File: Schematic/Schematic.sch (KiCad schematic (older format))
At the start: 13 parts, among them U1 74LS04, U10 HC-SR04, U11 HC-SR04, U12 HC-SR04, U13 HC-SR04, U2 74LS04, U3 74LS138, U4 ESP32-CAM, U5 HC-SR04, U6 HC-SR04, U7 HC-SR04, U8 HC-SR04, U9 DHT11

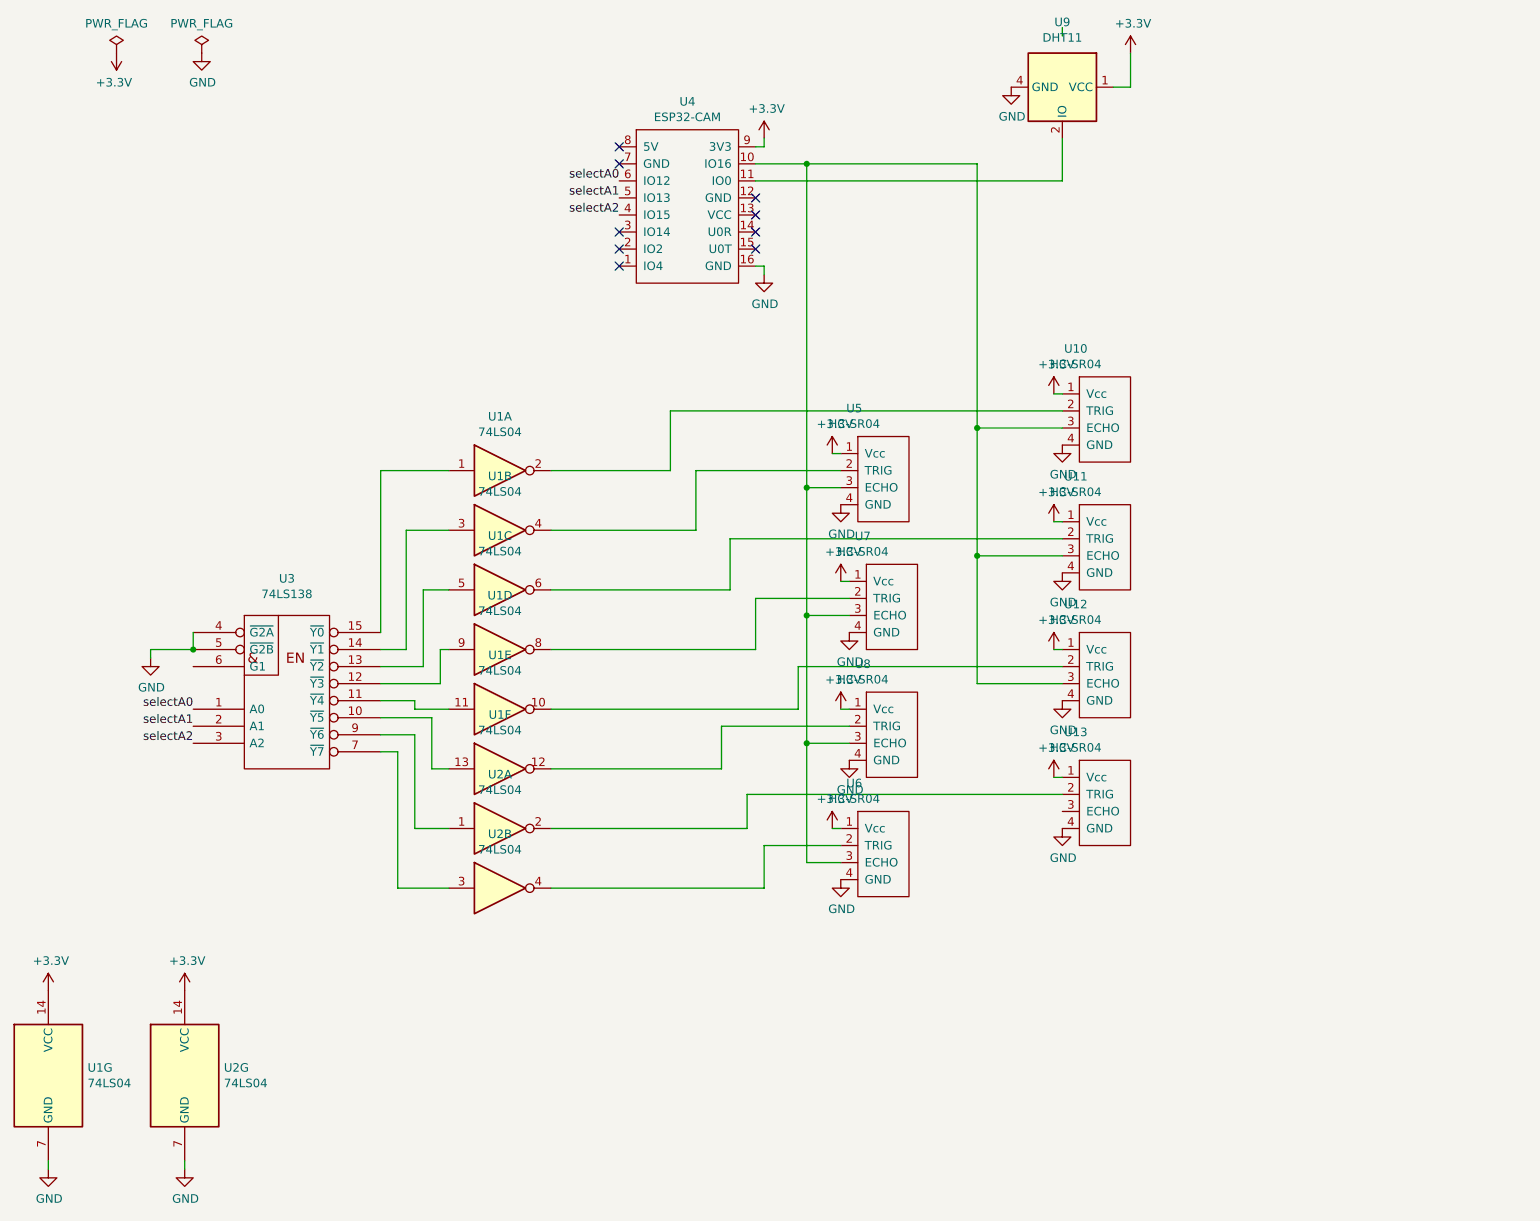
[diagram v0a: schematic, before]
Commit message: added a 8 to 1 mux to select the sensor to listen to
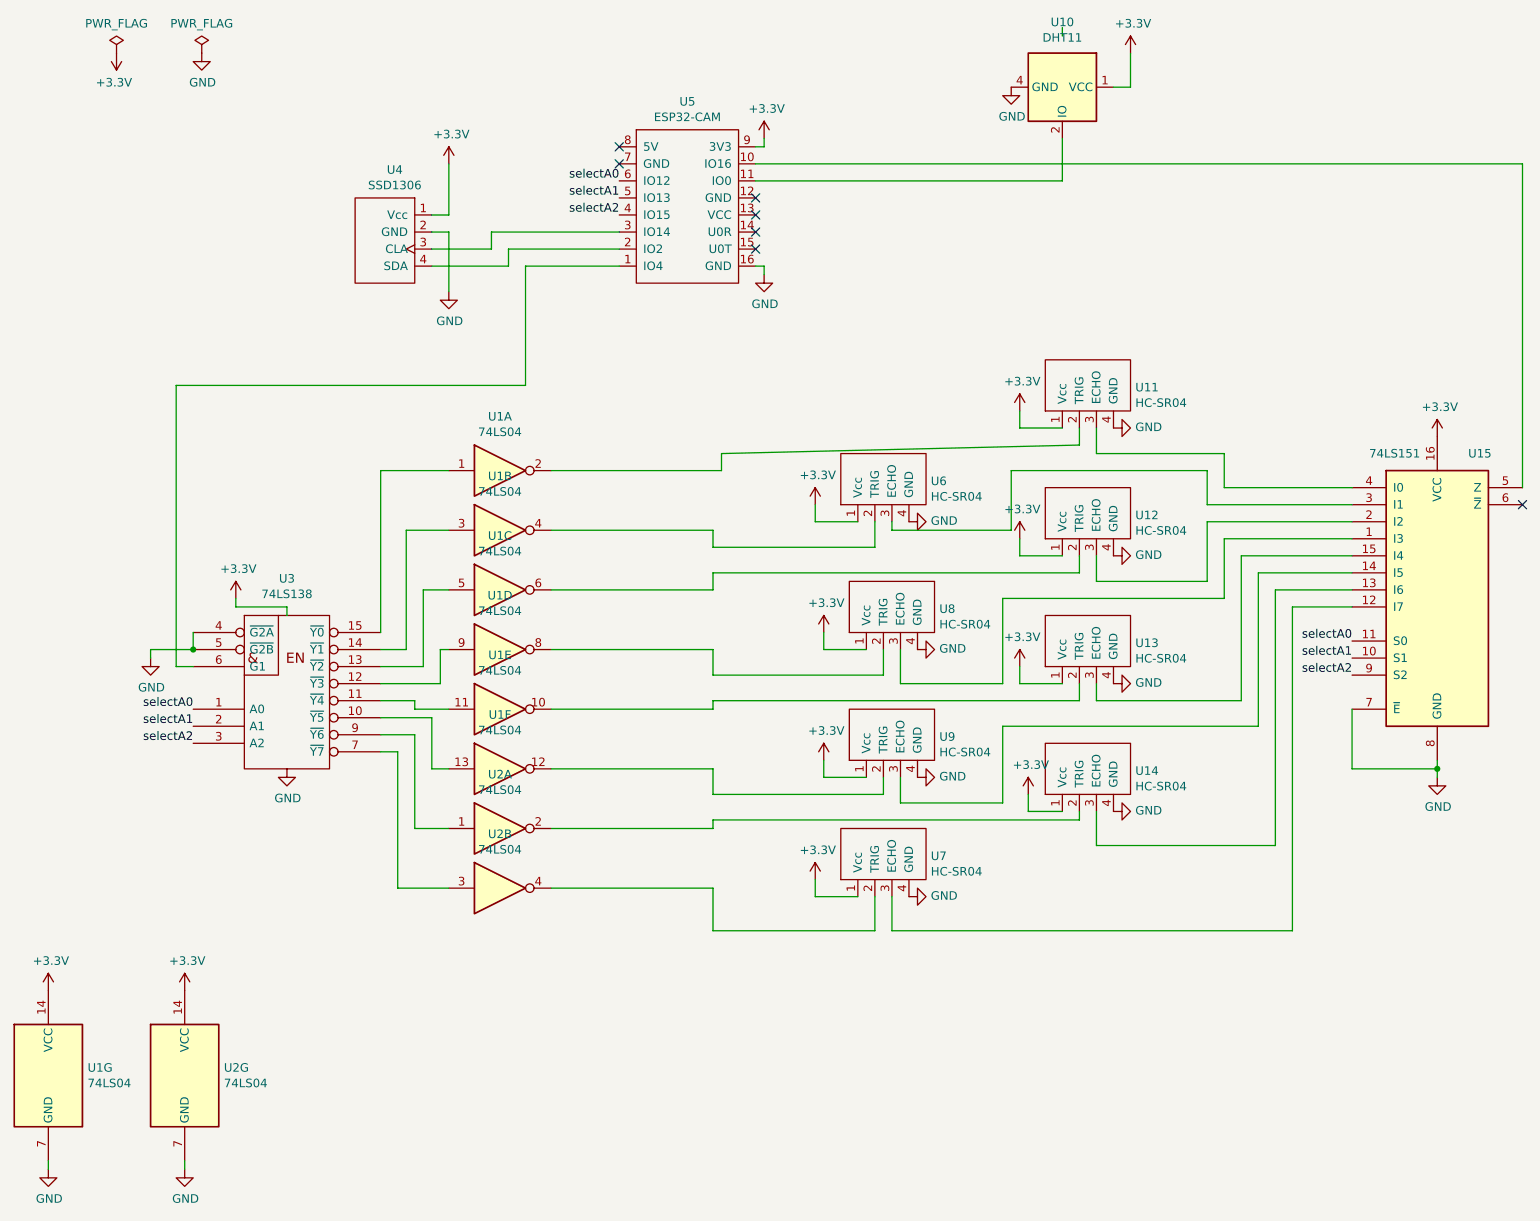
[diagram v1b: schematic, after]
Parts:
- added U15: 74LS151, symbol 74xx:74LS151
- added U4: SSD1306, symbol Project_Symbols:SSD1306
- renumbered U9 to U10, U10 to U11, U11 to U12, U12 to U13, U13 to U14, U4 to U5, U5 to U6, U6 to U7, U7 to U8, U8 to U9
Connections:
- net VCC is gone; now on net +3V3: U3.16 (VCC)
- net +3V3: now also U15.16 (VCC), U4.1 (Vcc)
- net GND: now also U15.7 (~E), U15.8 (GND), U4.2 (GND)
- net selectA0: now also U15.11 (S0)
- net selectA1: now also U15.10 (S1)
- net selectA2: now also U15.9 (S2)
- net at U3.6 (G1): now also U5.1 (IO4)
- net at U5.2 (IO2): now also U4.4 (SDA)
- net at U5.3 (IO14): now also U4.3 (CLA)
- net at U14.3 (ECHO): now also U15.13 (I6)
- new net: U15.5 (Z), U5.10 (IO16)
- new net: U15.3 (I1), U6.3 (ECHO)
- new net: U15.14 (I5), U9.3 (ECHO)
- new net: U12.3 (ECHO), U15.2 (I2)
- new net: U11.3 (ECHO), U15.4 (I0)
- new net: U15.1 (I3), U8.3 (ECHO)
- new net: U13.3 (ECHO), U15.15 (I4)
- new net: U15.12 (I7), U7.3 (ECHO)
- no-connect marks 9 -> 7
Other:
- moved on the sheet: U11, U12, U13, U14, U6, U7, U8, U9
